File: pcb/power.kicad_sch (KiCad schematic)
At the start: 40 parts, among them J1 XT30PW-M, Q1 NTR4003N, Q2 NTR4003N, Q3 Si3407DV, SW3 SLW-864574-5A-RA-N-D, U2 TPS561246DRLR, U3 ZXCT180A4W5

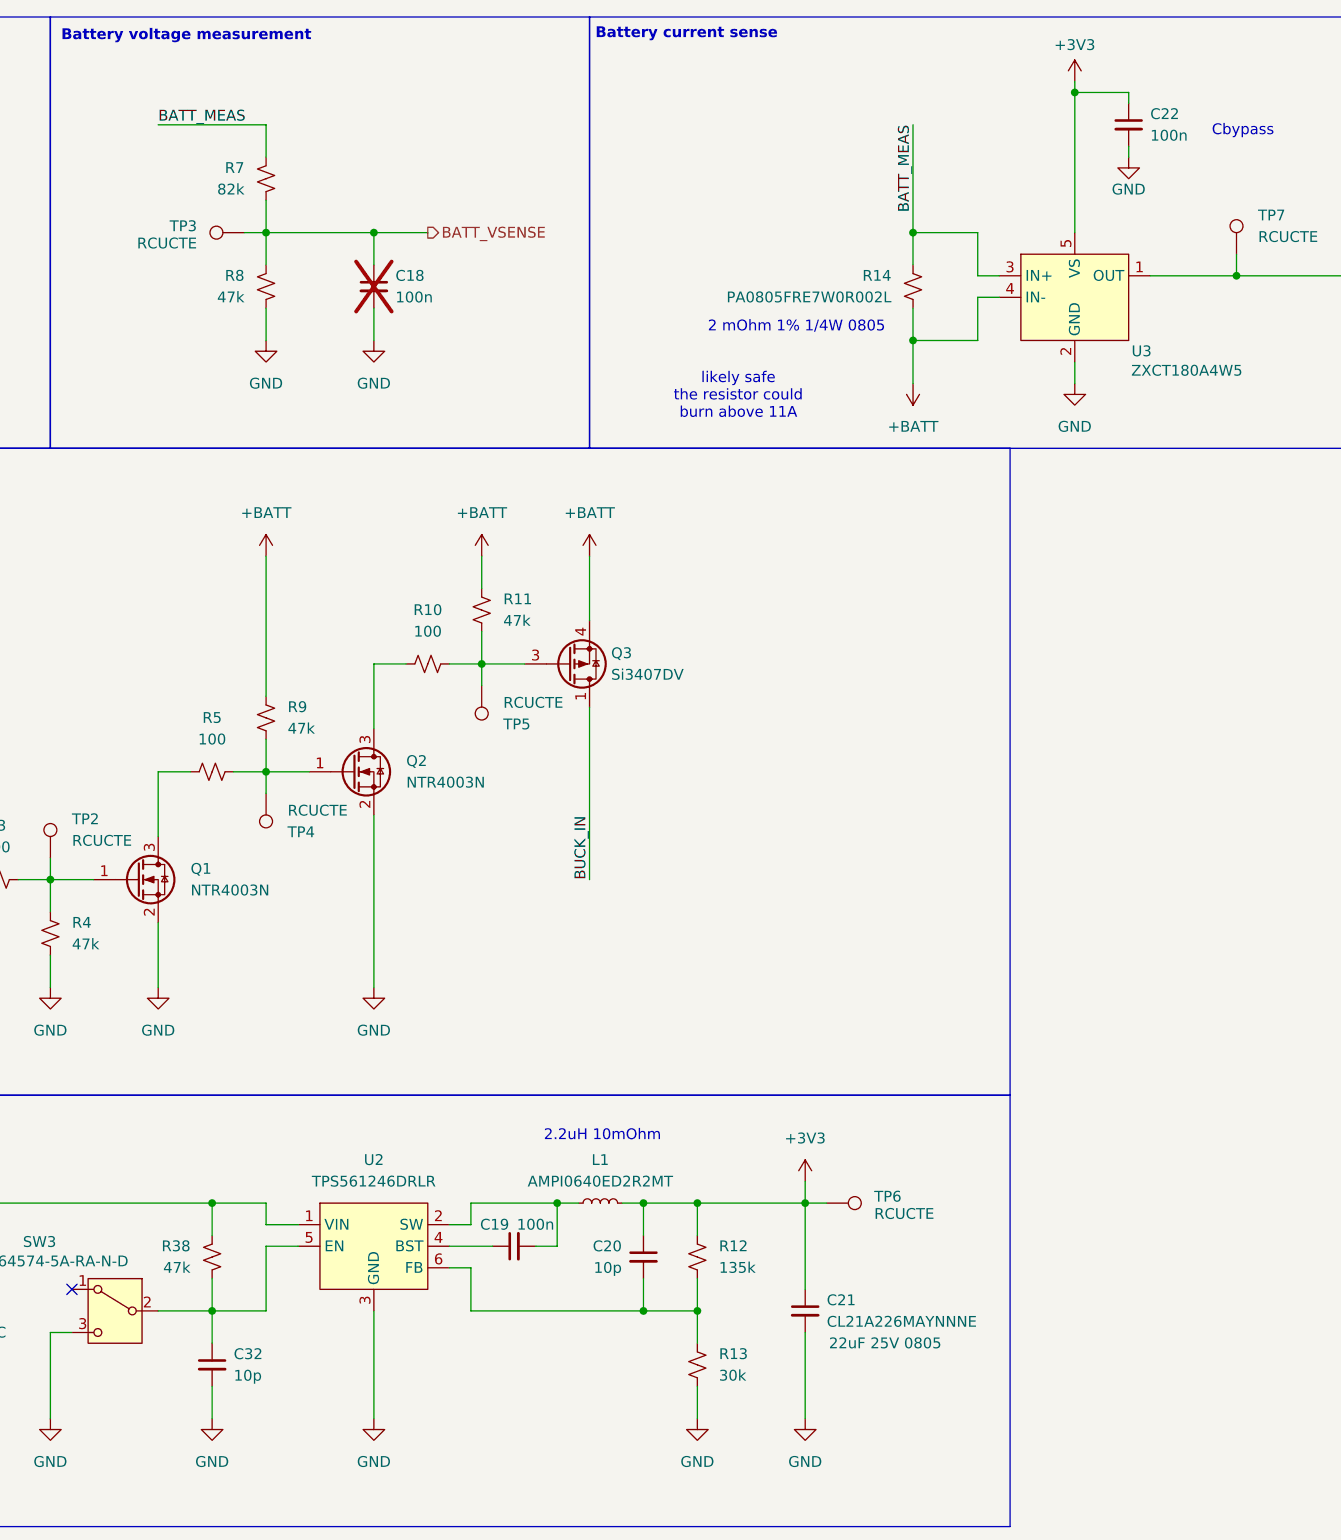
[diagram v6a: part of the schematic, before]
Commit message: Add buck enable switch
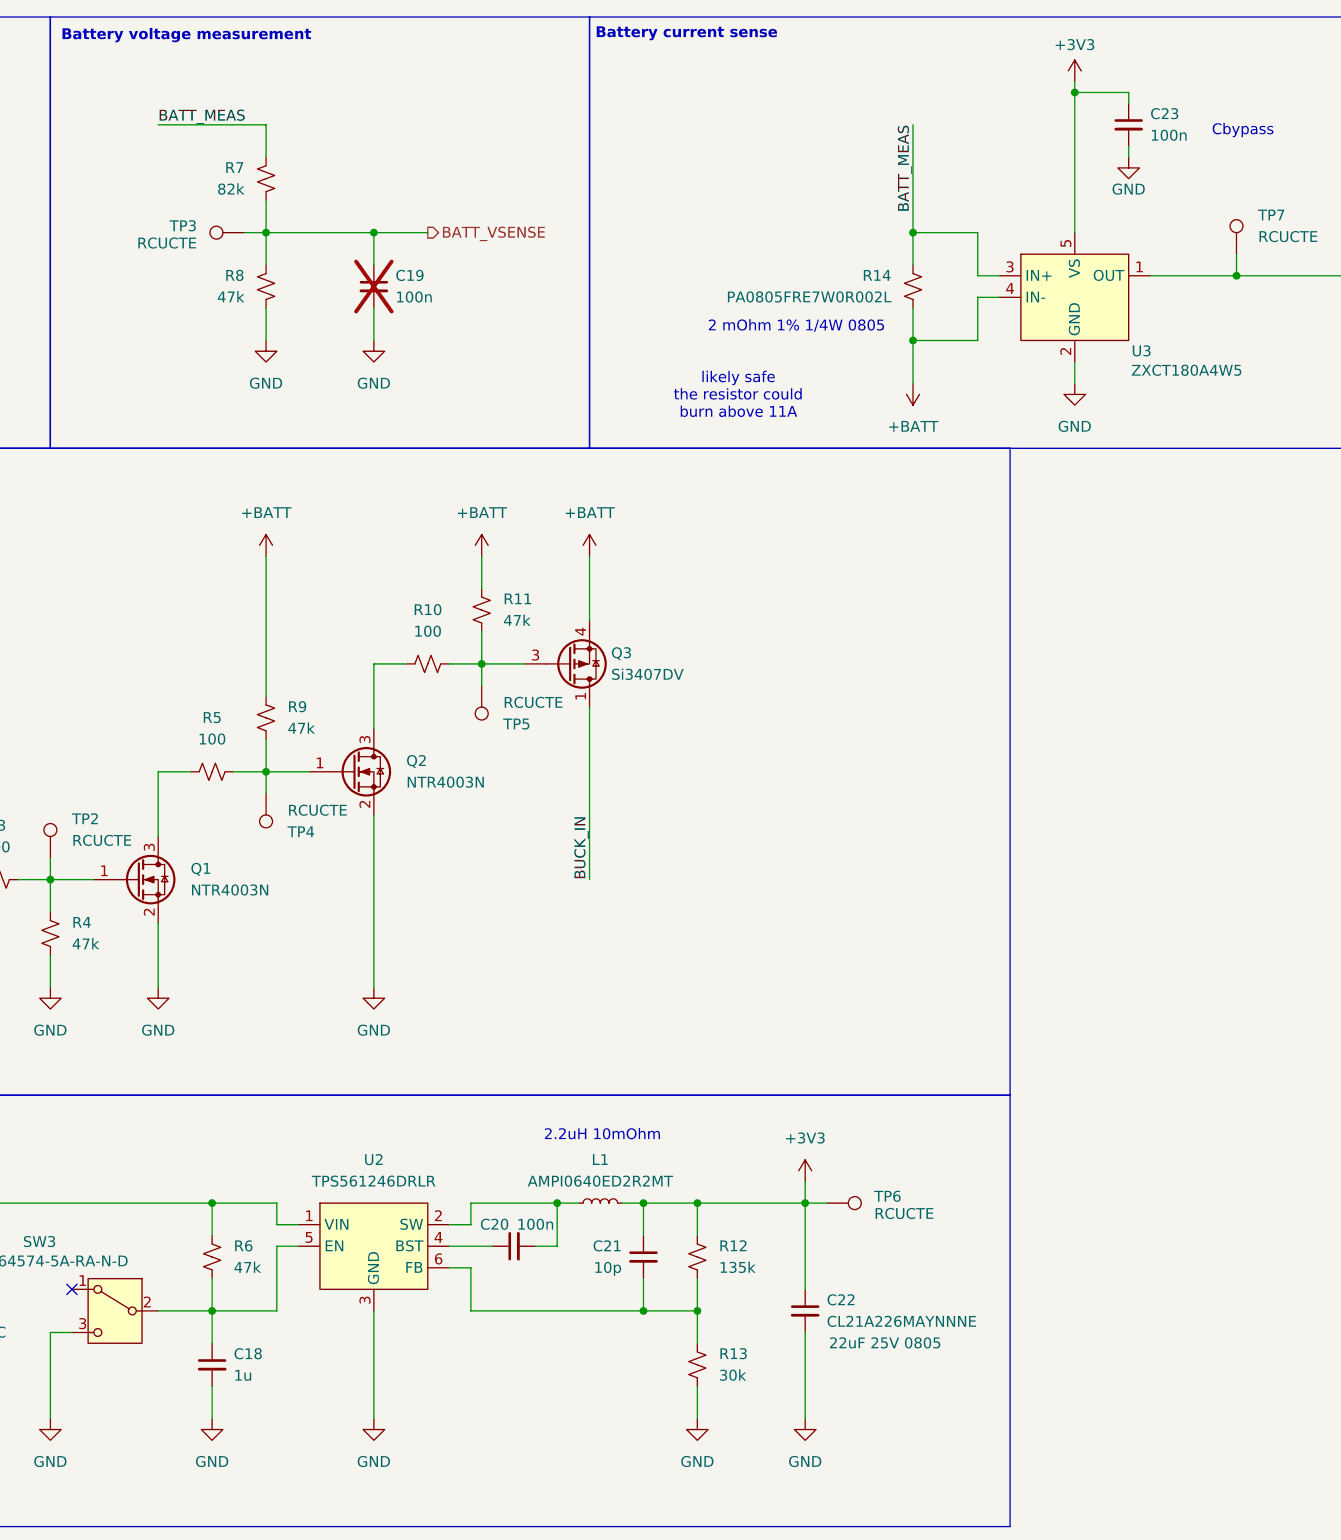
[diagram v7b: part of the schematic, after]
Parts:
- C18: renamed from C32; value 10p -> 1u
- SW3: footprint (none) -> SW_SameSky:SW_SameSky_SLW-864574-5A-RA-N-D
- renumbered C18 to C19, C19 to C20, C20 to C21, C21 to C22, C22 to C23, R38 to R6
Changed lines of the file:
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@@
 	(wire
 		(pts
-			(xy 92.71 157.48) (xy 88.9 157.48)
+			(xy 92.71 157.48) (xy 90.17 157.48)
 		)
 		(stroke
@@
 	(wire
 		(pts
-			(xy 88.9 157.48) (xy 88.9 165.1)
+			(xy 90.17 157.48) (xy 90.17 165.1)
 		)
 		(stroke
@@
 	(wire
 		(pts
-			(xy 88.9 152.4) (xy 88.9 154.94)
+			(xy 90.17 152.4) (xy 90.17 154.94)
 		)
 		(stroke
@@
 	(wire
 		(pts
-			(xy 88.9 154.94) (xy 92.71 154.94)
+			(xy 90.17 154.94) (xy 92.71 154.94)
 		)
 		(stroke
@@
 	(wire
 		(pts
-			(xy 82.55 152.4) (xy 88.9 152.4)
+			(xy 82.55 152.4) (xy 90.17 152.4)
 		)
 		(stroke
@@
 	(wire
 		(pts
-			(xy 88.9 165.1) (xy 82.55 165.1)
+			(xy 90.17 165.1) (xy 82.55 165.1)
 		)
 		(stroke
@@
 		(on_board yes)
 		(dnp no)
-		(property "Reference" "C19"
+		(property "Reference" "C20"
 			(at 115.824 154.94 90)
 			(effects
@@
 			(project ""
 				(path "/1f4fd4ed-9886-4375-a5ac-dc32d5760936/3ce152e6-c1c9-4db1-8237-913c82724d53"
-					(reference "C19")
+					(reference "C20")
 					(unit 1)
 				)
@@
 		(dnp no)
 		(fields_autoplaced yes)
-		(property "Reference" "#PWR038"
+		(property "Reference" "#PWR039"
 			(at 152.4 153.67 0)
 			(effects
@@
 			(project ""
 				(path "/1f4fd4ed-9886-4375-a5ac-dc32d5760936/3ce152e6-c1c9-4db1-8237-913c82724d53"
-					(reference "#PWR038")
+					(reference "#PWR039")
 					(unit 1)
 				)
@@
 		(dnp no)
 		(fields_autoplaced yes)
-		(property "Reference" "C22"
+		(property "Reference" "C23"
 			(at 193.04 24.1362 0)
 			(effects
@@
 			(project "airbrake_mod"
 				(path "/1f4fd4ed-9886-4375-a5ac-dc32d5760936/3ce152e6-c1c9-4db1-8237-913c82724d53"
-					(reference "C22")
+					(reference "C23")
 					(unit 1)
 				)
@@
 		(dnp yes)
 		(fields_autoplaced yes)
-		(property "Reference" "C18"
+		(property "Reference" "C19"
 			(at 104.14 43.1862 0)
 			(effects
@@
 			(project ""
 				(path "/1f4fd4ed-9886-4375-a5ac-dc32d5760936/3ce152e6-c1c9-4db1-8237-913c82724d53"
-					(reference "C18")
+					(reference "C19")
 					(unit 1)
 				)
@@
 		(on_board yes)
 		(dnp no)
-		(property "Reference" "C20"
+		(property "Reference" "C21"
 			(at 130.81 157.4862 0)
 			(effects
@@
 			(project "airbrake_mod"
 				(path "/1f4fd4ed-9886-4375-a5ac-dc32d5760936/3ce152e6-c1c9-4db1-8237-913c82724d53"
-					(reference "C20")
+					(reference "C21")
 					(unit 1)
 				)
@@
 		(dnp no)
 		(fields_autoplaced yes)
-		(property "Reference" "#PWR035"
+		(property "Reference" "#PWR036"
 			(at 114.3 80.01 0)
 			(effects
@@
 			(project "airbrake_mod"
 				(path "/1f4fd4ed-9886-4375-a5ac-dc32d5760936/3ce152e6-c1c9-4db1-8237-913c82724d53"
-					(reference "#PWR035")
+					(reference "#PWR036")
 					(unit 1)
 				)
@@
 		(on_board yes)
 		(dnp no)
-		(property "Reference" "C21"
+		(property "Reference" "C22"
 			(at 154.94 163.8362 0)
 			(effects
@@
 			(project "airbrake_mod"
 				(path "/1f4fd4ed-9886-4375-a5ac-dc32d5760936/3ce152e6-c1c9-4db1-8237-913c82724d53"
-					(reference "C21")
+					(reference "C22")
 					(unit 1)
 				)
@@
 		(dnp no)
 		(fields_autoplaced yes)
-		(property "Reference" "#PWR044"
+		(property "Reference" "#PWR045"
 			(at 254 26.67 0)
 			(effects
@@
 			(project ""
 				(path "/1f4fd4ed-9886-4375-a5ac-dc32d5760936/3ce152e6-c1c9-4db1-8237-913c82724d53"
-					(reference "#PWR044")
+					(reference "#PWR045")
 					(unit 1)
 				)
@@
 		(dnp no)
 		(fields_autoplaced yes)
-		(property "Reference" "#PWR091"
+		(property "Reference" "#PWR030"
 			(at 82.55 184.15 0)
 			(effects
@@
 			(project "airbrake_mod"
 				(path "/1f4fd4ed-9886-4375-a5ac-dc32d5760936/3ce152e6-c1c9-4db1-8237-913c82724d53"
-					(reference "#PWR091")
+					(reference "#PWR030")
 					(unit 1)
 				)
@@
 		(dnp no)
 		(fields_autoplaced yes)
-		(property "Reference" "#PWR031"
+		(property "Reference" "#PWR032"
 			(at 88.9 80.01 0)
 			(effects
@@
 			(project ""
 				(path "/1f4fd4ed-9886-4375-a5ac-dc32d5760936/3ce152e6-c1c9-4db1-8237-913c82724d53"
-					(reference "#PWR031")
+					(reference "#PWR032")
 					(unit 1)
 				)
@@
 		(dnp no)
 		(fields_autoplaced yes)
-		(property "Reference" "#PWR039"
+		(property "Reference" "#PWR040"
 			(at 152.4 184.15 0)
 			(effects
@@
 			(project "airbrake_mod"
 				(path "/1f4fd4ed-9886-4375-a5ac-dc32d5760936/3ce152e6-c1c9-4db1-8237-913c82724d53"
-					(reference "#PWR039")
+					(reference "#PWR040")
 					(unit 1)
 				)
@@
 		(dnp no)
 		(fields_autoplaced yes)
-		(property "Reference" "#PWR034"
+		(property "Reference" "#PWR035"
 			(at 101.6 184.15 0)
 			(effects
@@
 			(project ""
 				(path "/1f4fd4ed-9886-4375-a5ac-dc32d5760936/3ce152e6-c1c9-4db1-8237-913c82724d53"
-					(reference "#PWR034")
+					(reference "#PWR035")
 					(unit 1)
 				)
@@
 		(dnp no)
 		(fields_autoplaced yes)
-		(property "Reference" "#PWR036"
+		(property "Reference" "#PWR037"
 			(at 127 80.01 0)
 			(effects
@@
 			(project "airbrake_mod"
 				(path "/1f4fd4ed-9886-4375-a5ac-dc32d5760936/3ce152e6-c1c9-4db1-8237-913c82724d53"
-					(reference "#PWR036")
+					(reference "#PWR037")
 					(unit 1)
 				)
@@
 		(on_board yes)
 		(dnp no)
-		(property "Reference" "C32"
+		(property "Reference" "C18"
 			(at 85.09 170.1862 0)
 			(effects
@@
 			)
 		)
-		(property "Value" "10p"
+		(property "Value" "1u"
 			(at 85.09 172.7262 0)
 			(effects
@@
 			(project "airbrake_mod"
 				(path "/1f4fd4ed-9886-4375-a5ac-dc32d5760936/3ce152e6-c1c9-4db1-8237-913c82724d53"
-					(reference "C32")
+					(reference "C18")
 					(unit 1)
 				)
@@
 		(dnp no)
 		(fields_autoplaced yes)
-		(property "Reference" "#PWR046"
+		(property "Reference" "#PWR047"
 			(at 254 59.69 0)
 			(effects
@@
 			(project "airbrake_mod"
 				(path "/1f4fd4ed-9886-4375-a5ac-dc32d5760936/3ce152e6-c1c9-4db1-8237-913c82724d53"
-					(reference "#PWR046")
+					(reference "#PWR047")
 					(unit 1)
 				)
@@
 		(lib_id "Device:R_Small_US")
 		(at 82.55 158.75 0)
-		(mirror y)
 		(unit 1)
 		(exclude_from_sim no)
@@
 		(on_board yes)
 		(dnp no)
-		(property "Reference" "R38"
-			(at 80.01 157.4799 0)
+		(property "Reference" "R6"
+			(at 85.09 157.4799 0)
 			(effects
 				(font
@@
 		)
 		(property "Value" "47k"
-			(at 80.01 160.0199 0)
+			(at 85.09 160.0199 0)
 			(effects
 				(font
@@
 			(project "airbrake_mod"
 				(path "/1f4fd4ed-9886-4375-a5ac-dc32d5760936/3ce152e6-c1c9-4db1-8237-913c82724d53"
-					(reference "R38")
+					(reference "R6")
 					(unit 1)
 				)
@@
 		(on_board yes)
 		(dnp no)
-		(property "Reference" "#PWR043"
+		(property "Reference" "#PWR044"
 			(at 190.5 35.56 0)
 			(effects
@@
 			(project "airbrake_mod"
 				(path "/1f4fd4ed-9886-4375-a5ac-dc32d5760936/3ce152e6-c1c9-4db1-8237-913c82724d53"
-					(reference "#PWR043")
+					(reference "#PWR044")
 					(unit 1)
 				)
@@
 		(on_board yes)
 		(dnp no)
-		(property "Reference" "#PWR041"
+		(property "Reference" "#PWR042"
 			(at 184.15 24.13 0)
 			(effects
@@
 			(project "airbrake_mod"
 				(path "/1f4fd4ed-9886-4375-a5ac-dc32d5760936/3ce152e6-c1c9-4db1-8237-913c82724d53"
-					(reference "#PWR041")
+					(reference "#PWR042")
 					(unit 1)
 				)
@@
 		(dnp no)
 		(fields_autoplaced yes)
-		(property "Reference" "#PWR033"
+		(property "Reference" "#PWR034"
 			(at 101.6 133.35 0)
 			(effects
@@
 			(project "airbrake_mod"
 				(path "/1f4fd4ed-9886-4375-a5ac-dc32d5760936/3ce152e6-c1c9-4db1-8237-913c82724d53"
-					(reference "#PWR033")
+					(reference "#PWR034")
 					(unit 1)
 				)
@@
 		(dnp no)
 		(fields_autoplaced yes)
-		(property "Reference" "#PWR037"
+		(property "Reference" "#PWR038"
 			(at 139.7 184.15 0)
 			(effects
@@
 			(project "airbrake_mod"
 				(path "/1f4fd4ed-9886-4375-a5ac-dc32d5760936/3ce152e6-c1c9-4db1-8237-913c82724d53"
-					(reference "#PWR037")
+					(reference "#PWR038")
 					(unit 1)
 				)
@@
 		(dnp no)
 		(fields_autoplaced yes)
-		(property "Reference" "#PWR042"
+		(property "Reference" "#PWR043"
 			(at 184.15 62.23 0)
 			(effects
@@
 			(project "airbrake_mod"
 				(path "/1f4fd4ed-9886-4375-a5ac-dc32d5760936/3ce152e6-c1c9-4db1-8237-913c82724d53"
-					(reference "#PWR042")
+					(reference "#PWR043")
 					(unit 1)
 				)
@@
 		(dnp no)
 		(fields_autoplaced yes)
-		(property "Reference" "#PWR047"
+		(property "Reference" "#PWR048"
 			(at 254 72.39 0)
 			(effects
@@
 			(project ""
 				(path "/1f4fd4ed-9886-4375-a5ac-dc32d5760936/3ce152e6-c1c9-4db1-8237-913c82724d53"
-					(reference "#PWR047")
+					(reference "#PWR048")
 					(unit 1)
 				)
@@
 		(dnp no)
 		(fields_autoplaced yes)
-		(property "Reference" "#PWR032"
+		(property "Reference" "#PWR033"
 			(at 101.6 57.15 0)
 			(effects
@@
 			(project "airbrake_mod"
 				(path "/1f4fd4ed-9886-4375-a5ac-dc32d5760936/3ce152e6-c1c9-4db1-8237-913c82724d53"
-					(reference "#PWR032")
+					(reference "#PWR033")
 					(unit 1)
 				)
@@
 			)
 		)
-		(property "Footprint" ""
+		(property "Footprint" "SW_SameSky:SW_SameSky_SLW-864574-5A-RA-N-D"
 			(at 71.12 165.1 0)
 			(effects
@@
 		(dnp no)
 		(fields_autoplaced yes)
-		(property "Reference" "#PWR045"
+		(property "Reference" "#PWR046"
 			(at 254 39.37 0)
 			(effects
@@
 			(project "airbrake_mod"
 				(path "/1f4fd4ed-9886-4375-a5ac-dc32d5760936/3ce152e6-c1c9-4db1-8237-913c82724d53"
-					(reference "#PWR045")
+					(reference "#PWR046")
 					(unit 1)
 				)
@@
 		(dnp no)
 		(fields_autoplaced yes)
-		(property "Reference" "#PWR040"
+		(property "Reference" "#PWR041"
 			(at 165.1 52.07 0)
 			(effects
@@
 			(project "airbrake_mod"
 				(path "/1f4fd4ed-9886-4375-a5ac-dc32d5760936/3ce152e6-c1c9-4db1-8237-913c82724d53"
-					(reference "#PWR040")
+					(reference "#PWR041")
 					(unit 1)
 				)
@@
 		(dnp no)
 		(fields_autoplaced yes)
-		(property "Reference" "#PWR030"
+		(property "Reference" "#PWR031"
 			(at 88.9 57.15 0)
 			(effects
@@
 			(project "airbrake_mod"
 				(path "/1f4fd4ed-9886-4375-a5ac-dc32d5760936/3ce152e6-c1c9-4db1-8237-913c82724d53"
-					(reference "#PWR030")
+					(reference "#PWR031")
 					(unit 1)
 				)

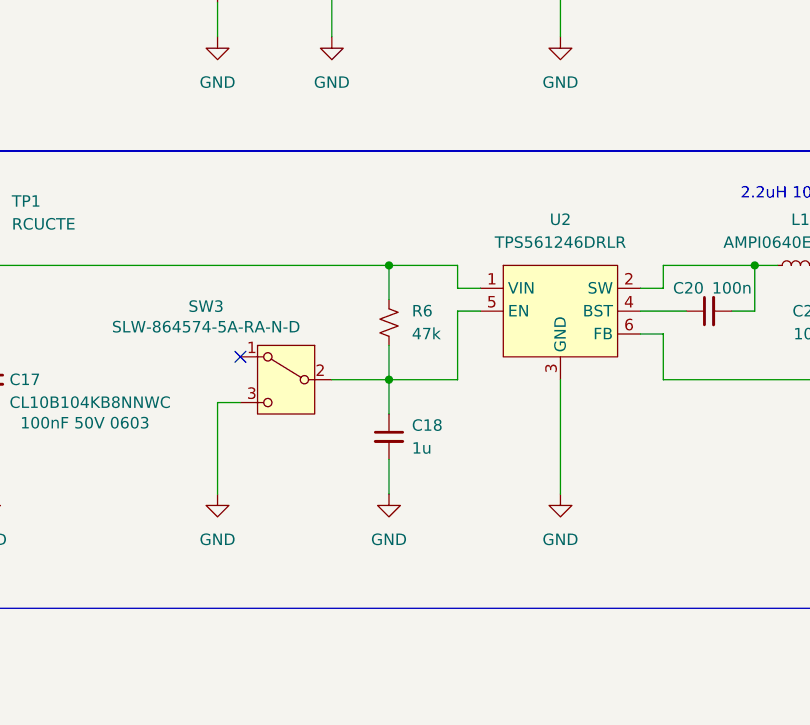
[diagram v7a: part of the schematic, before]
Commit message: Annotate buck EN details
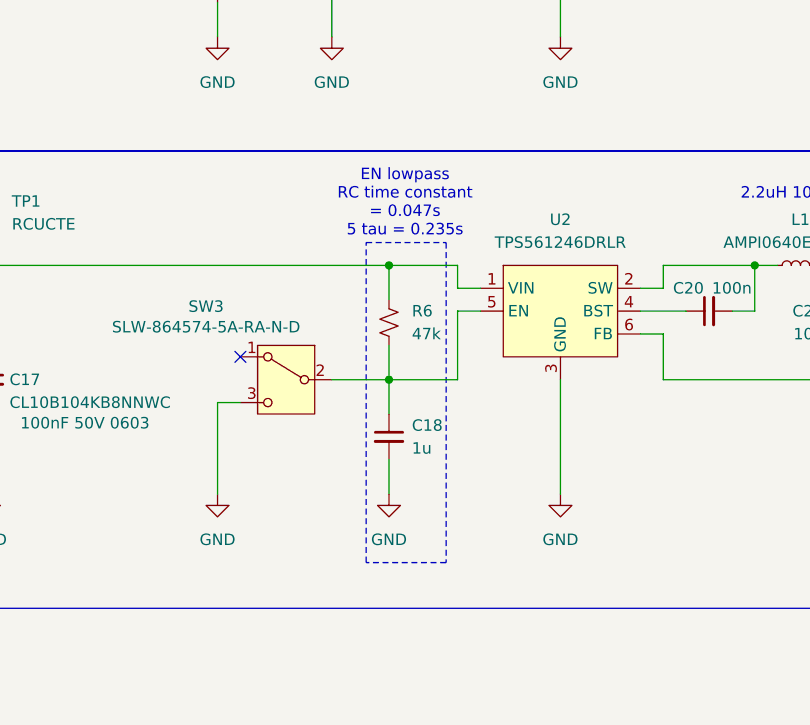
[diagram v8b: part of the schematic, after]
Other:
- note added: "EN lowpass RC time constant = 0.047s 5 tau = 0.235s"
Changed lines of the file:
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@@
+		)
+	)
+	(rectangle
+		(start 80.01 149.86)
+		(end 88.9 185.42)
+		(stroke
+			(width 0)
+			(type dot)
+		)
+		(fill
+			(type none)
 		)
 	)
@@
 		(effects
 			(font
+				(size 1.27 1.27)
+			)
+		)
+	)
+	(text "EN lowpass\nRC time constant\n= 0.047s\n5 tau = 0.235s"
+		(exclude_from_sim no)
+		(at 84.328 145.542 0)
+		(effects
+			(font
